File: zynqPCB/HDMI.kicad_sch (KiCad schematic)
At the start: 25 parts, among them J3 Micro_SD_Card_Det, U16 FTDITypeUART, U17 ABRACON-ASDMB, U18 S25FL256SAGNFI001, U20 xc7z020clg484

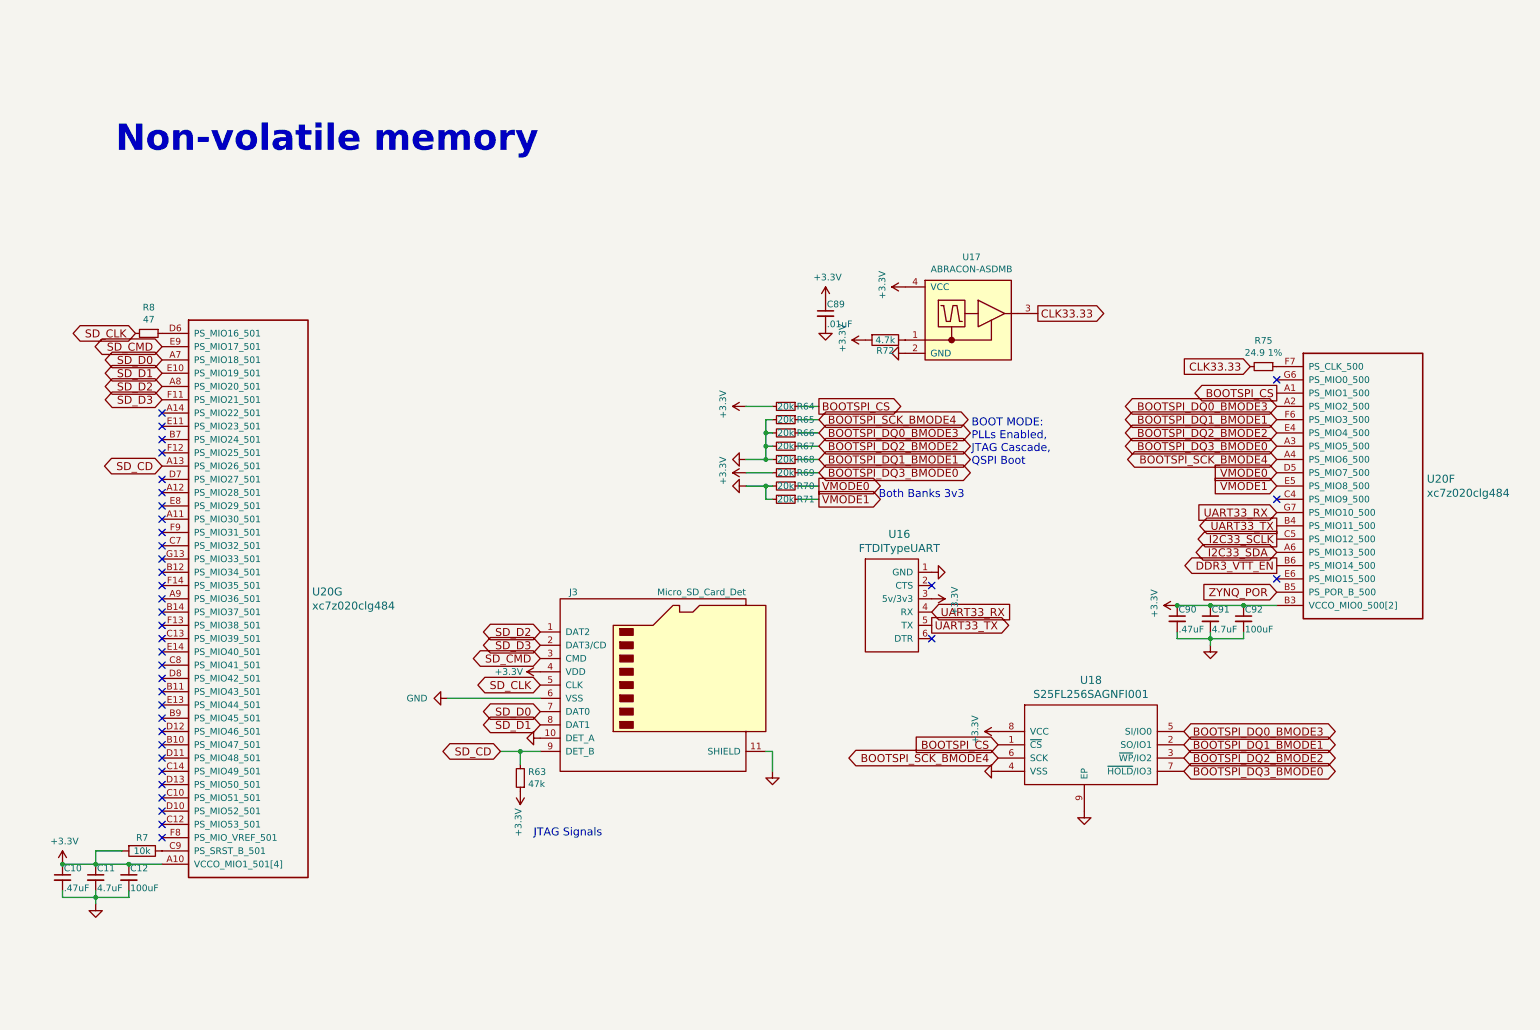
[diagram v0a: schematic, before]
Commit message: Sanity Checks and added some footprints
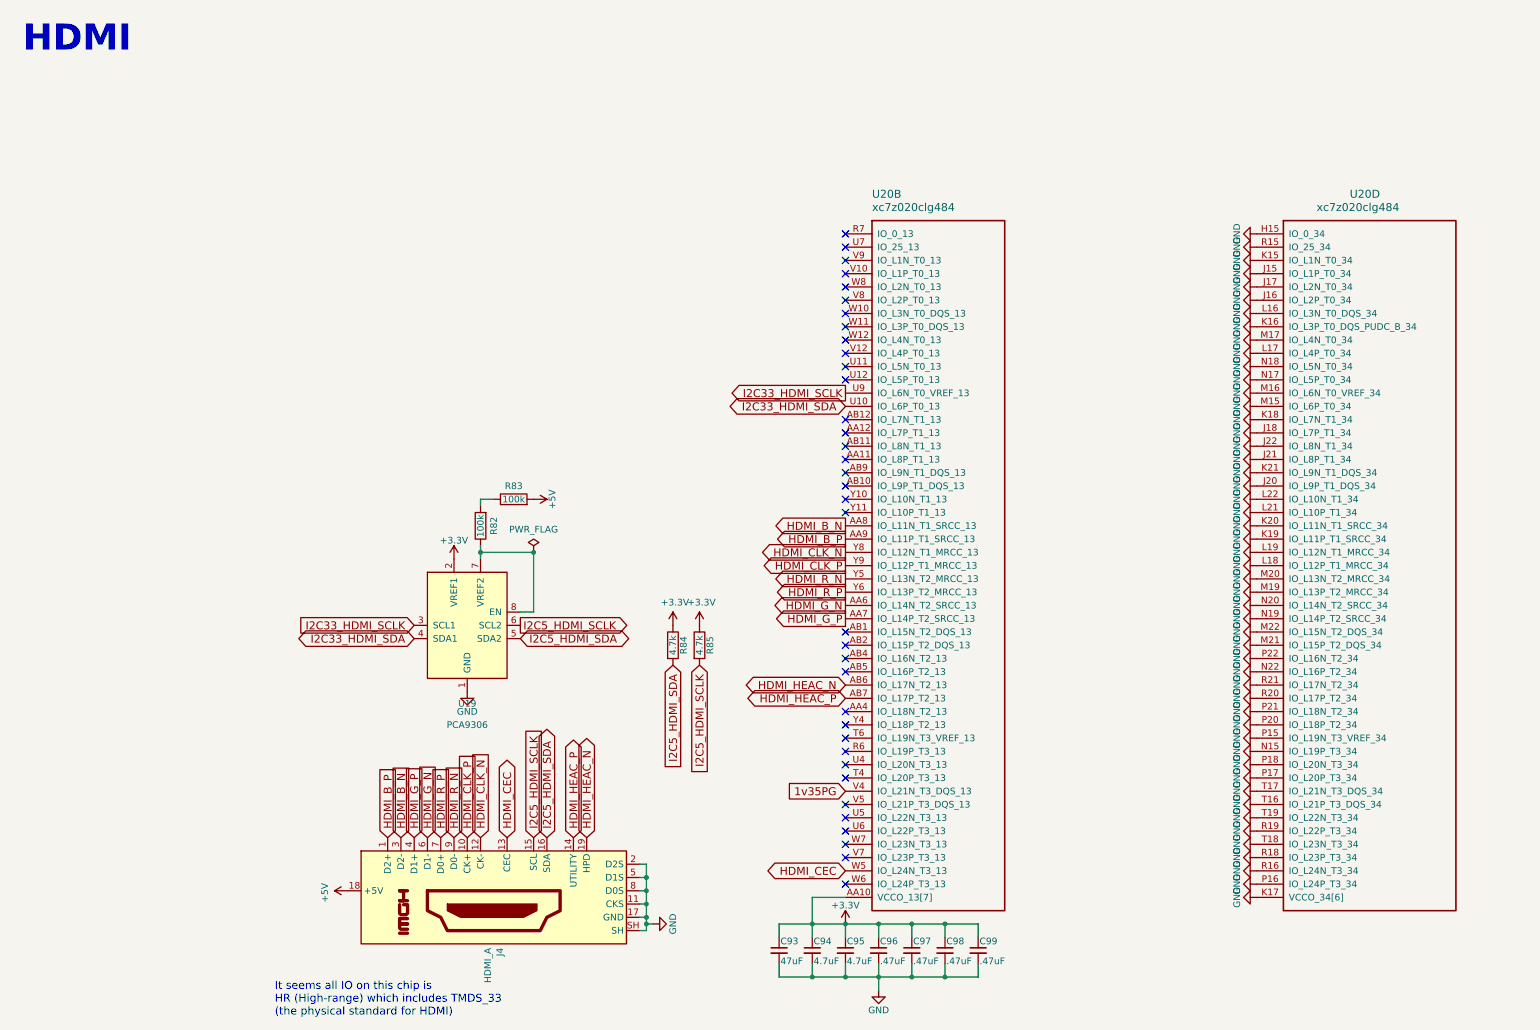
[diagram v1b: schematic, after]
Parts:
- removed C10, C90: .47uF, Capacitor_SMD:C_0402_1005Metric, symbol Device:C_Small
- removed C11, C91: 4.7uF, Capacitor_SMD:C_0402_1005Metric, symbol Device:C_Small
- removed C12, C92: 100uF, Capacitor_SMD:C_1210_3225Metric, symbol Device:C_Small
- removed C89: .01uF, Capacitor_SMD:C_0402_1005Metric, symbol Device:C_Small
- removed J3: Micro_SD_Card_Det, DFTcustom:AMPHENOL-114-00841-68, symbol DFTBoard-rescue:Micro_SD_Card_Det-
- removed R63: 47k, Resistor_SMD:R_0402_1005Metric, symbol Device:R_Small
- removed R64, R65, R66, R67, R68, R69, R70, R71: 20k, Resistor_SMD:R_0402_1005Metric, symbol Device:R_Small
- removed R7: 10k, Resistor_SMD:R_0402_1005Metric, symbol Device:R
- removed R72: 4.7k, Resistor_SMD:R_0402_1005Metric, symbol Device:R
- removed R75: 24.9 1%, Resistor_SMD:R_0402_1005Metric, symbol Device:R_Small
- removed R8: 47, Resistor_SMD:R_0402_1005Metric, symbol Device:R_Small
- removed U16: FTDITypeUART, DFTcustom:FTDI_CONN, symbol DFTCustom:FTDITypeUART
- removed U17: ABRACON-ASDMB, XTAL_ASDMB-24.000MHZ-LC-T:XTAL_ASDMB-24.000MHZ-LC-T, symbol Abracon:ABRACON-ASDMB
- removed U18: S25FL256SAGNFI001, DFTcustom:WNG008_SPA-L, symbol DFTBoard-rescue:S25FL256SAGNFI001-parts
- removed U20: xc7z020clg484, DFTcustom:BGA-484_19.0x19.0mm_Layout22x22_P0.80mm_dia0.40mm, symbol xilinx7:xc7z020clg484
- added C93: 47uF, Capacitor_SMD:C_1210_3225Metric, symbol Device:C_Small
- added C94, C95: 4.7uF, Capacitor_SMD:C_0402_1005Metric, symbol Device:C_Small
- added C96, C97, C98, C99: .47uF, Capacitor_SMD:C_0402_1005Metric, symbol Device:C_Small
- added J4: HDMI_A, DFTcustom:10029449-111RLF, symbol Connector:HDMI_A
- added R82, R83: 100k, Resistor_SMD:R_0402_1005Metric, symbol Device:R
- added R84, R85: 4.7k, Resistor_SMD:R_0402_1005Metric, symbol Device:R
- added U19: PCA9306, Package_SO:SSOP-8_2.95x2.8mm_P0.65mm, symbol Interface:PCA9306
- added U20: xc7z020clg484, DFTcustom:BGA-484_19.0x19.0mm_Layout22x22_P0.80mm_dia0.40mm, symbol xilinx7:xc7z020clg484
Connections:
- net +3.3V: now also C93.1, C94.1, C95.1, C96.1, C97.1, C98.1, C99.1, R84.1, R85.1, U19.2 (VREF1), U20.AA10 (VCCO_13[7]), U20.AB3 (VCCO_13[7]), U20.T5 (VCCO_13[7]), U20.U8 (VCCO_13[7]), U20.V11 (VCCO_13[7]), U20.W4 (VCCO_13[7]), U20.Y7 (VCCO_13[7])
- net GND: now also C93.2, C94.2, C95.2, C96.2, C97.2, C98.2, C99.2, J4.11 (CKS), J4.17 (GND), J4.2 (D2S), J4.5 (D1S), J4.8 (D0S), J4.SH, U19.1 (GND), U20.H15 (IO_0_34), U20.J15 (IO_L1P_T0_34), U20.J16 (IO_L2P_T0_34), U20.J17 (IO_L2N_T0_34), U20.J18 (IO_L7P_T1_34), U20.J20 (IO_L9P_T1_DQS_34), U20.J21 (IO_L8P_T1_34), U20.J22 (IO_L8N_T1_34), U20.K15 (IO_L1N_T0_34), U20.K16 (IO_L3P_T0_DQS_PUDC_B_34), U20.K17 (VCCO_34[6]), U20.K18 (IO_L7N_T1_34), U20.K19 (IO_L11P_T1_SRCC_34), U20.K20 (IO_L11N_T1_SRCC_34), U20.K21 (IO_L9N_T1_DQS_34), U20.L16 (IO_L3N_T0_DQS_34), U20.L17 (IO_L4P_T0_34), U20.L18 (IO_L12P_T1_MRCC_34), U20.L19 (IO_L12N_T1_MRCC_34), U20.L20 (VCCO_34[6]), U20.L21 (IO_L10P_T1_34), U20.L22 (IO_L10N_T1_34), U20.M15 (IO_L6P_T0_34), U20.M16 (IO_L6N_T0_VREF_34), U20.M17 (IO_L4N_T0_34), U20.M19 (IO_L13P_T2_MRCC_34), U20.M20 (IO_L13N_T2_MRCC_34), U20.M21 (IO_L15P_T2_DQS_34), U20.M22 (IO_L15N_T2_DQS_34), U20.N15 (IO_L19P_T3_34), U20.N16 (VCCO_34[6]), U20.N17 (IO_L5P_T0_34), U20.N18 (IO_L5N_T0_34), U20.N19 (IO_L14P_T2_SRCC_34), U20.N20 (IO_L14N_T2_SRCC_34), U20.N22 (IO_L16P_T2_34), U20.P15 (IO_L19N_T3_VREF_34), U20.P16 (IO_L24P_T3_34), U20.P17 (IO_L20P_T3_34), U20.P18 (IO_L20N_T3_34), U20.P19 (VCCO_34[6]), U20.P20 (IO_L18P_T2_34), U20.P21 (IO_L18N_T2_34), U20.P22 (IO_L16N_T2_34), U20.R15 (IO_25_34), U20.R16 (IO_L24N_T3_34), U20.R18 (IO_L23P_T3_34), U20.R19 (IO_L22P_T3_34), U20.R20 (IO_L17P_T2_34), U20.R21 (IO_L17N_T2_34), U20.R22 (VCCO_34[6]), U20.T15 (VCCO_34[6]), U20.T16 (IO_L21P_T3_DQS_34), U20.T17 (IO_L21N_T3_DQS_34), U20.T18 (IO_L23N_T3_34), U20.T19 (IO_L22N_T3_34)
- new net: R82.1, U19.7 (VREF2), U19.8 (EN)
- new net: R82.2, R83.1
- new net +5V: J4.18 (+5V), R83.2
- new net 1v35PG: U20.V4 (IO_L21N_T3_DQS_13)
- new net HDMI_B_N: J4.3 (D2-), U20.AA8 (IO_L11N_T1_SRCC_13)
- new net HDMI_B_P: J4.1 (D2+), U20.AA9 (IO_L11P_T1_SRCC_13)
- new net HDMI_CEC: J4.13 (CEC), U20.W5 (IO_L24N_T3_13)
- new net HDMI_CLK_N: J4.12 (CK-), U20.Y8 (IO_L12N_T1_MRCC_13)
- new net HDMI_CLK_P: J4.10 (CK+), U20.Y9 (IO_L12P_T1_MRCC_13)
- new net HDMI_G_N: J4.6 (D1-), U20.AA6 (IO_L14N_T2_SRCC_13)
- new net HDMI_G_P: J4.4 (D1+), U20.AA7 (IO_L14P_T2_SRCC_13)
- new net HDMI_HEAC_N: J4.19 (HPD), U20.AB6 (IO_L17N_T2_13)
- new net HDMI_HEAC_P: J4.14 (UTILITY), U20.AB7 (IO_L17P_T2_13)
- new net HDMI_R_N: J4.9 (D0-), U20.Y5 (IO_L13N_T2_MRCC_13)
- new net HDMI_R_P: J4.7 (D0+), U20.Y6 (IO_L13P_T2_MRCC_13)
- new net I2C33_HDMI_SCLK: U19.3 (SCL1), U20.U9 (IO_L6N_T0_VREF_13)
- new net I2C33_HDMI_SDA: U19.4 (SDA1), U20.U10 (IO_L6P_T0_13)
- new net I2C5_HDMI_SCLK: J4.15 (SCL), R85.2, U19.6 (SCL2)
- new net I2C5_HDMI_SDA: J4.16 (SDA), R84.2, U19.5 (SDA2)
- no-connect marks 37 -> 36
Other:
- note added: "HDMI"
- note added: "It seems all IO on this chip is HR (High-range) which includes TMDS_33 (the physical standard for HDMI)"
- note removed: "BOOT MODE: PLLs Enabled, JTAG Cascade, QSPI Boot"
- note removed: "Both Banks 3v3"
- note removed: "JTAG Signals"
- note removed: "Non-volatile memory"
